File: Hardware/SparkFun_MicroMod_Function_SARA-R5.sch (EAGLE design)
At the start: 92 parts, among them IC2 SN74AVC4T774PW, J1 MICROMOD_FUNCTION_STANDARD, J2 U.FL, J4 U.FL, J9 NANO_SIM, Q2 310mA/60V/1.6Ω, Q3 310mA/60V/1.6Ω, Q5 310mA/60V/1.6Ω, Q6 310mA/60V/1.6Ω, U1 SARA-R510M8S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

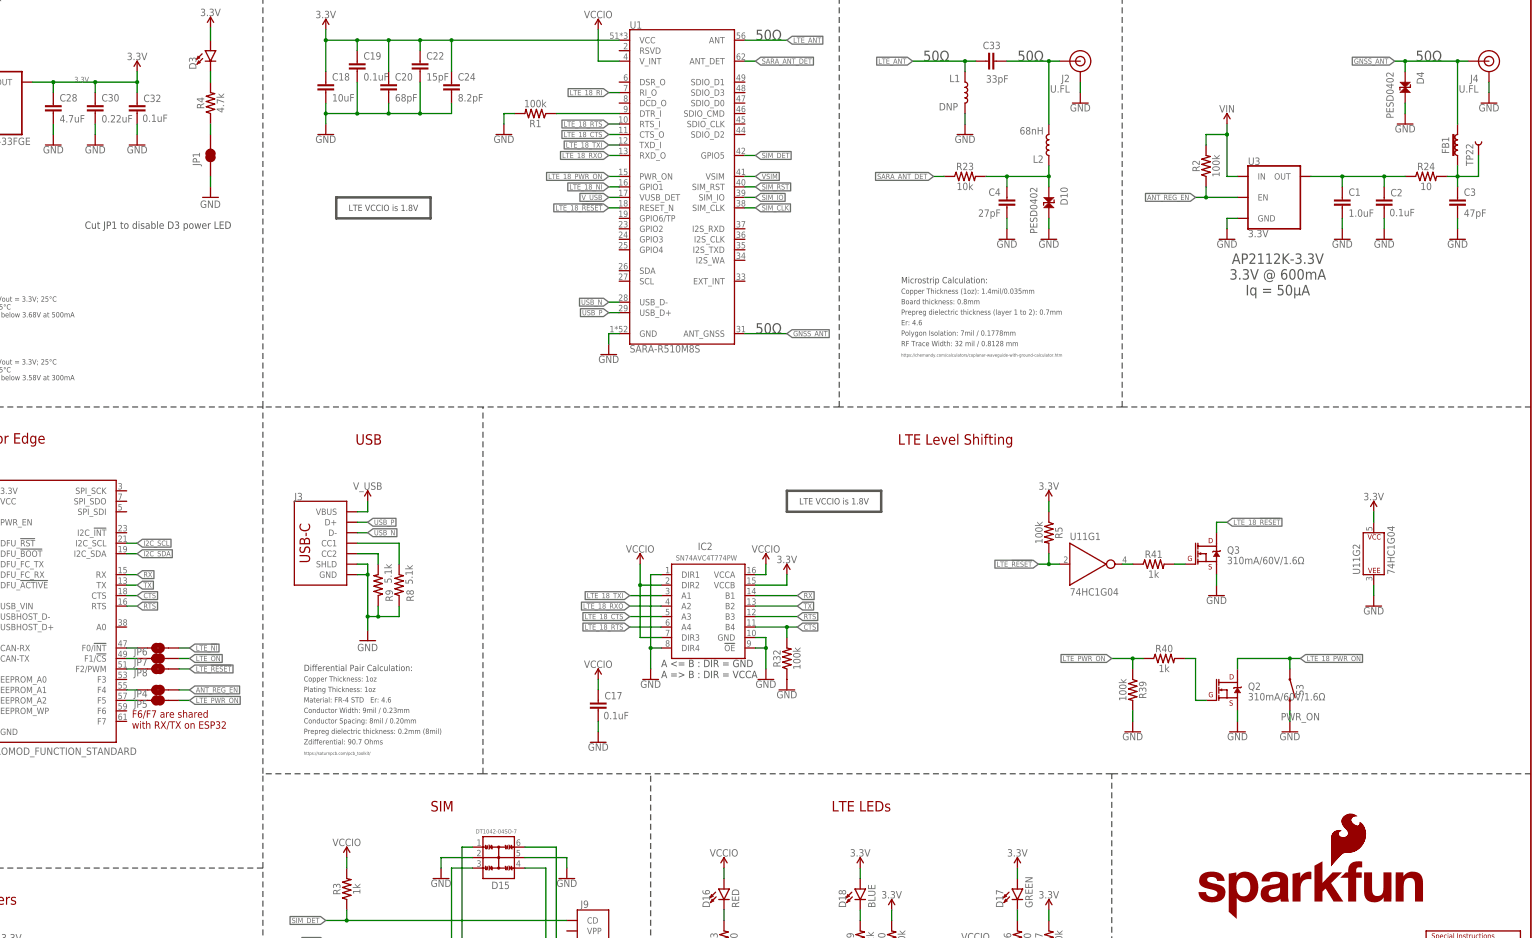
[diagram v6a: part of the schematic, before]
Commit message: added oshw logo
-also added label to ANT_REG_EN jumper
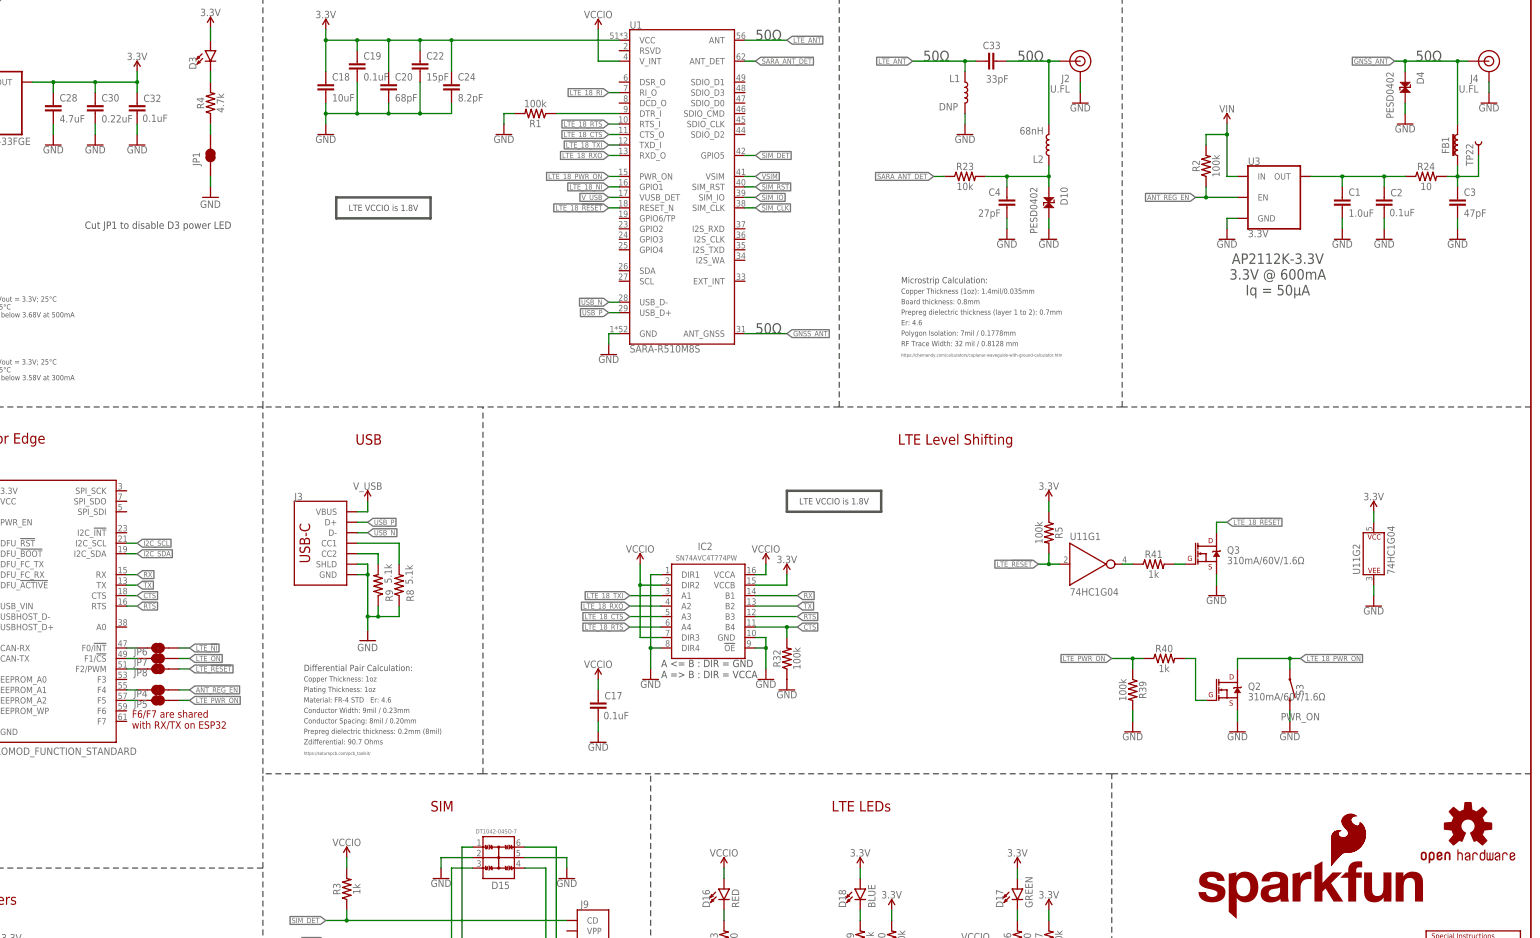
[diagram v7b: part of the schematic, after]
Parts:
- added LOGO4: OSHW-LOGOMINI, SparkFun-Aesthetics:OSHW-LOGOMINI
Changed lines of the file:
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@@
 <part name="GND50" library="SparkFun-PowerSymbols" deviceset="GND" device=""/>
 <part name="SUPPLY17" library="SparkFun-PowerSymbols" deviceset="VIN" device=""/>
+<part name="LOGO4" library="SparkFun-Aesthetics" deviceset="OSHW-LOGO" device="MINI"/>
 </parts>
 <sheets>
@@
 <text x="243.84" y="185.42" size="2.54" layer="97" font="vector">50Ω</text>
 <wire x1="330.2" y1="35.56" x2="330.2" y2="78.74" width="0.2032" layer="97" style="longdash"/>
-<text x="134.366" y="98.552" size="1.27" layer="97">Plating Thickness: 1oz</text>
-<text x="134.366" y="96.012" size="1.27" layer="97">Material: FR-4 STD   Er: 4.6</text>
-<text x="134.366" y="101.092" size="1.27" layer="97">Copper Thickness: 1oz</text>
-<text x="134.366" y="90.932" size="1.27" layer="97">Conductor Spacing: 8mil / 0.20mm</text>
-<text x="134.366" y="93.472" size="1.27" layer="97">Conductor Width: 9mil / 0.23mm</text>
-<text x="134.366" y="88.392" size="1.27" layer="97">Prepreg dielectric thickness: 0.2mm (8mil)</text>
-<text x="134.366" y="83.312" size="0.762" layer="97">https://saturnpcb.com/pcb_toolkit/</text>
-<text x="134.366" y="103.632" size="1.524" layer="97" ratio="15">Differential Pair Calculation:</text>
-<text x="134.366" y="85.852" size="1.27" layer="97">Zdifferential: 90.7 Ohms</text>
+<text x="134.366" y="98.552" size="1.27" layer="97" font="vector">Plating Thickness: 1oz</text>
+<text x="134.366" y="96.012" size="1.27" layer="97" font="vector">Material: FR-4 STD   Er: 4.6</text>
+<text x="134.366" y="101.092" size="1.27" layer="97" font="vector">Copper Thickness: 1oz</text>
+<text x="134.366" y="90.932" size="1.27" layer="97" font="vector">Conductor Spacing: 8mil / 0.20mm</text>
+<text x="134.366" y="93.472" size="1.27" layer="97" font="vector">Conductor Width: 9mil / 0.23mm</text>
+<text x="134.366" y="88.392" size="1.27" layer="97" font="vector">Prepreg dielectric thickness: 0.2mm (8mil)</text>
+<text x="134.366" y="83.312" size="0.762" layer="97" font="vector">https://saturnpcb.com/pcb_toolkit/</text>
+<text x="134.366" y="103.632" size="1.524" layer="97" font="vector" ratio="15">Differential Pair Calculation:</text>
+<text x="134.366" y="85.852" size="1.27" layer="97" font="vector">Zdifferential: 90.7 Ohms</text>
 </plain>
 <instances>
@@
 <attribute name="VALUE" x="48.26" y="251.714" size="1.778" layer="96" font="vector" align="bottom-center"/>
 </instance>
+<instance part="LOGO4" gate="G$1" x="416.56" y="66.04" smashed="yes"/>
 </instances>
 <busses>
@@
 <junction x="73.66" y="246.38"/>
 <junction x="93.98" y="246.38"/>
-<label x="78.74" y="246.38" size="1.27" layer="95" font="vector"/>
 </segment>
 <segment>

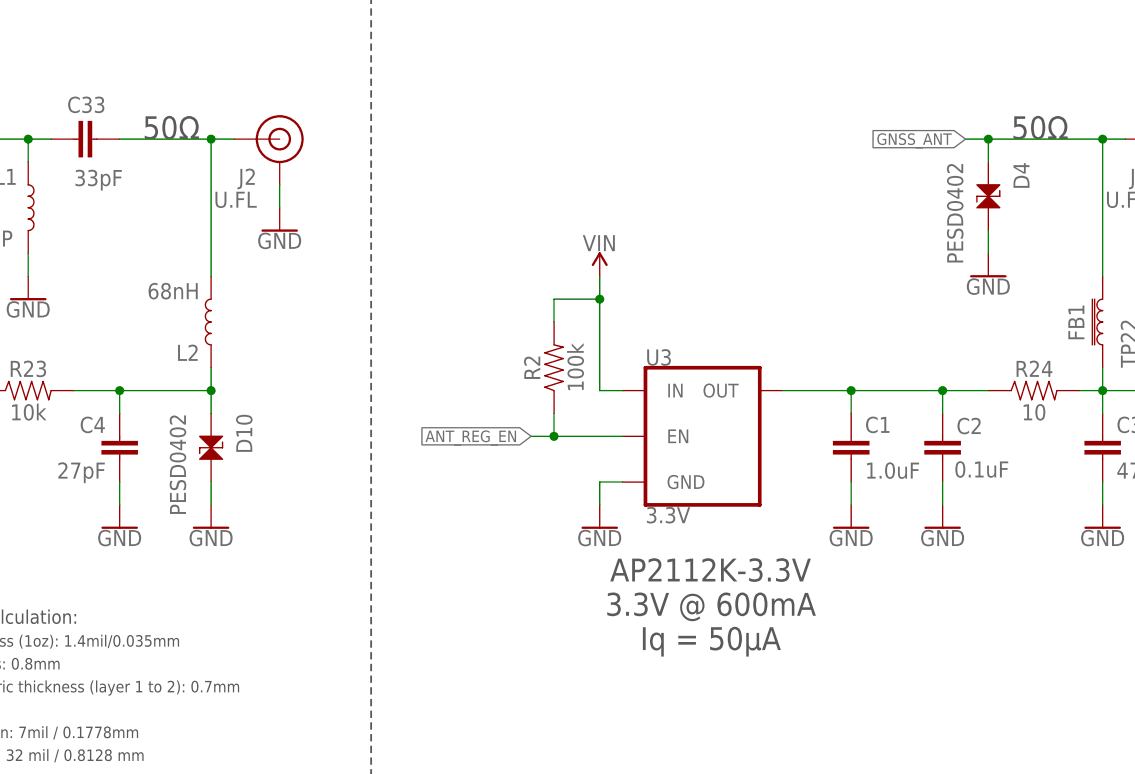
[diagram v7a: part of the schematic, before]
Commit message: library work
-switching some parts over to SFE libraries
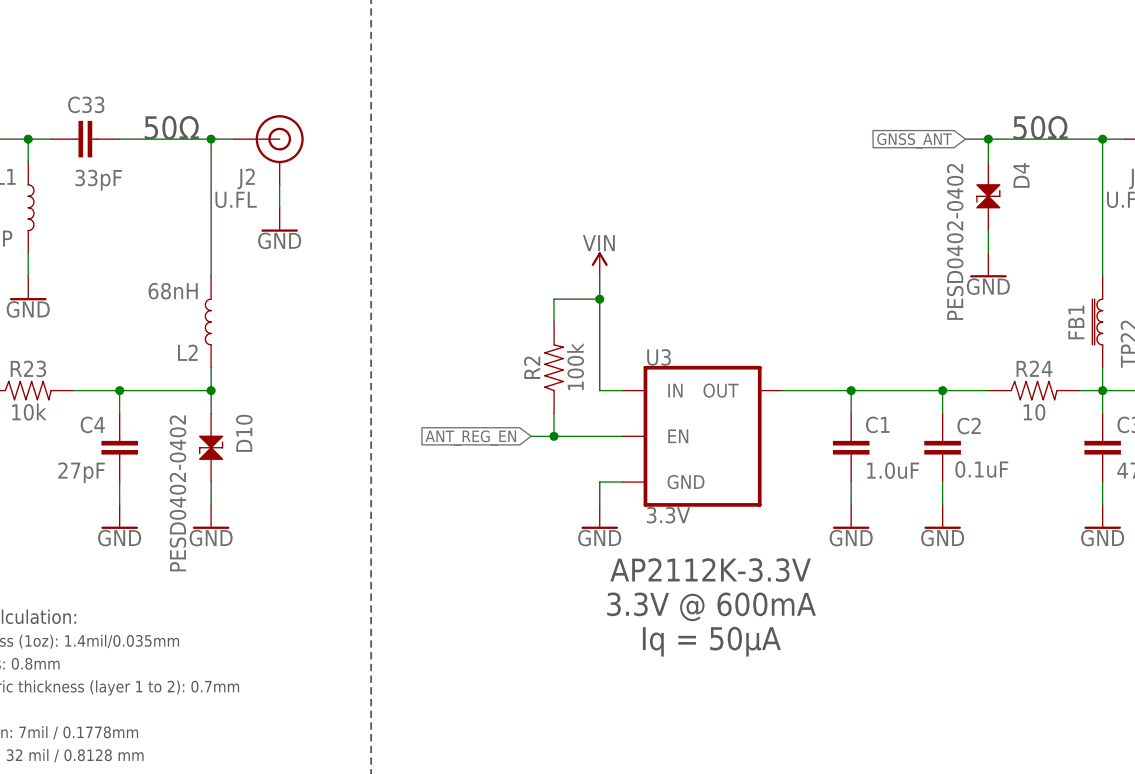
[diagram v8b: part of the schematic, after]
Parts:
- C33: device New_Parts:33PF-0402-25V-5%-X7R -> SparkFun-Capacitors:33PF-0402T-50V-5%
- C4: device New_Parts:27PF-0402-25V-5%-X7R -> SparkFun-Capacitors:27PF-0402-50V-5%
- D10, D4: value PESD0402 -> PESD0402-0402; device New_Parts:PESD0402 -> SparkFun-DiscreteSemi:PESD0402-0402
- D15: device ublox:TVS_DIODE_ARRAY_4DT1042-04SO-7 -> SparkFun-DiscreteSemi:TVS_DIODE_ARRAY_4_ESDA6V1BC6
- IC2: device New_Parts:SN74AVC4T774PW -> SparkFun-IC-Comms:SN74AVC4T774PW
- L2: device New_Parts:68NH-0402 -> SparkFun-Coils:68NH-0402-200MA
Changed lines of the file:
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@@
 <part name="GND33" library="SparkFun-PowerSymbols" deviceset="GND" device=""/>
 <part name="GND44" library="SparkFun-PowerSymbols" deviceset="GND" device=""/>
-<part name="D15" library="ublox" deviceset="TVS_DIODE_ARRAY_4" device="DT1042-04SO-7" value="DT1042-04SO-7"/>
+<part name="D15" library="SparkFun-DiscreteSemi" deviceset="TVS_DIODE_ARRAY_4" device="_ESDA6V1BC6" value="DT1042-04SO-7"/>
 <part name="GND34" library="SparkFun-PowerSymbols" deviceset="GND" device=""/>
 <part name="GND42" library="SparkFun-PowerSymbols" deviceset="GND" device=""/>
@@
 <part name="L1" library="New_Parts" deviceset="INDUCTOR_DNP" device="-0402" value="DNP"/>
 <part name="GND45" library="SparkFun-PowerSymbols" deviceset="GND" device=""/>
-<part name="C33" library="New_Parts" deviceset="33PF" device="-0402-25V-5%-X7R" value="33pF"/>
+<part name="C33" library="SparkFun-Capacitors" deviceset="33PF" device="-0402T-50V-5%" value="33pF"/>
 <part name="SUPPLY24" library="SparkFun-PowerSymbols" deviceset="VCCIO" device=""/>
 <part name="SUPPLY30" library="SparkFun-PowerSymbols" deviceset="VCCIO" device=""/>
@@
 <part name="R47" library="SparkFun-Resistors" deviceset="100KOHM" device="-0402T-1/16W-1%" value="100k"/>
 <part name="C22" library="SparkFun-Capacitors" library_urn="urn:adsk.eagle:library:510" deviceset="15PF" device="-0603-50V-5%" package3d_urn="urn:adsk.eagle:package:37414/1" value="15pF"/>
-<part name="IC2" library="New_Parts" deviceset="SN74AVC4T774PW" device=""/>
+<part name="IC2" library="SparkFun-IC-Comms" deviceset="SN74AVC4T774PW" device="" value="SN74AVC4T774PW"/>
 <part name="GND56" library="SparkFun-PowerSymbols" deviceset="GND" device=""/>
 <part name="GND70" library="SparkFun-PowerSymbols" deviceset="GND" device=""/>
@@
 <part name="C3" library="SparkFun-Capacitors" deviceset="47PF" device="-0603-50V-5%" value="47pF"/>
 <part name="GND54" library="SparkFun-PowerSymbols" deviceset="GND" device=""/>
-<part name="D4" library="New_Parts" deviceset="PESD0402" device=""/>
+<part name="D4" library="SparkFun-DiscreteSemi" deviceset="PESD0402" device="-0402"/>
 <part name="GND57" library="SparkFun-PowerSymbols" deviceset="GND" device=""/>
 <part name="TP22" library="SparkFun-Connectors" deviceset="TEST-POINT" device="3" value="TEST-POINT3"/>
@@
 <part name="R2" library="SparkFun-Resistors" deviceset="100KOHM" device="-0402T-1/16W-1%" value="100k"/>
 <part name="J4" library="SparkFun-Connectors" deviceset="U.FL2PIN" device="" value="U.FL"/>
-<part name="L2" library="New_Parts" deviceset="68NH" device="-0402" value="68nH"/>
-<part name="C4" library="New_Parts" deviceset="27PF" device="-0402-25V-5%-X7R" value="27pF"/>
+<part name="L2" library="SparkFun-Coils" deviceset="68NH" device="-0402-200MA" value="68nH"/>
+<part name="C4" library="SparkFun-Capacitors" deviceset="27PF" device="-0402-50V-5%" value="27pF"/>
 <part name="R23" library="SparkFun-Resistors" deviceset="10KOHM" device="-0603-1/10W-1%" value="10k"/>
 <part name="GND46" library="SparkFun-PowerSymbols" deviceset="GND" device=""/>
-<part name="D10" library="New_Parts" deviceset="PESD0402" device=""/>
+<part name="D10" library="SparkFun-DiscreteSemi" deviceset="PESD0402" device="-0402"/>
 <part name="GND50" library="SparkFun-PowerSymbols" deviceset="GND" device=""/>
 <part name="SUPPLY17" library="SparkFun-PowerSymbols" deviceset="VIN" device=""/>
@@
 <attribute name="VALUE" x="414.02" y="208.026" size="1.778" layer="96" font="vector" align="top-center"/>
 </instance>
-<instance part="D4" gate="G$1" x="401.32" y="246.38" smashed="yes" rot="R270">
+<instance part="D4" gate="D1" x="401.32" y="246.38" smashed="yes" rot="R270">
 <attribute name="NAME" x="404.114" y="248.92" size="1.778" layer="95" font="vector" rot="R270"/>
 <attribute name="VALUE" x="398.526" y="248.92" size="1.778" layer="96" font="vector" rot="R270" align="top-left"/>
@@
 <attribute name="VALUE" x="304.8" y="208.026" size="1.778" layer="96" font="vector" align="top-center"/>
 </instance>
-<instance part="D10" gate="G$1" x="314.96" y="218.44" smashed="yes" rot="R270">
+<instance part="D10" gate="D1" x="314.96" y="218.44" smashed="yes" rot="R270">
 <attribute name="NAME" x="317.754" y="220.98" size="1.778" layer="95" font="vector" rot="R270"/>
 <attribute name="VALUE" x="312.166" y="220.98" size="1.778" layer="96" font="vector" rot="R270" align="top-left"/>
@@
 <segment>
 <pinref part="GND57" gate="1" pin="GND"/>
-<pinref part="D4" gate="G$1" pin="2"/>
+<pinref part="D4" gate="D1" pin="2"/>
 <wire x1="401.32" y1="238.76" x2="401.32" y2="241.3" width="0.1524" layer="91"/>
 </segment>
@@
 <segment>
 <pinref part="GND50" gate="1" pin="GND"/>
-<pinref part="D10" gate="G$1" pin="2"/>
+<pinref part="D10" gate="D1" pin="2"/>
 <wire x1="314.96" y1="210.82" x2="314.96" y2="213.36" width="0.1524" layer="91"/>
 </segment>
@@
 <wire x1="414.02" y1="236.22" x2="414.02" y2="251.46" width="0.1524" layer="91"/>
 <junction x="414.02" y="251.46"/>
-<pinref part="D4" gate="G$1" pin="1"/>
+<pinref part="D4" gate="D1" pin="1"/>
 <wire x1="401.32" y1="248.92" x2="401.32" y2="251.46" width="0.1524" layer="91"/>
 <junction x="401.32" y="251.46"/>
@@
 <pinref part="C4" gate="G$1" pin="1"/>
 <wire x1="304.8" y1="223.52" x2="304.8" y2="220.98" width="0.1524" layer="91"/>
-<pinref part="D10" gate="G$1" pin="1"/>
+<pinref part="D10" gate="D1" pin="1"/>
 <wire x1="314.96" y1="220.98" x2="314.96" y2="223.52" width="0.1524" layer="91"/>
 <wire x1="314.96" y1="223.52" x2="304.8" y2="223.52" width="0.1524" layer="91"/>
